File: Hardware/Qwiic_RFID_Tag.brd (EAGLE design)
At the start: 25.4 x 50.8 mm, 49 parts, among them J1 Qwiic, J2 Qwiic, U1 ST25DV64KC

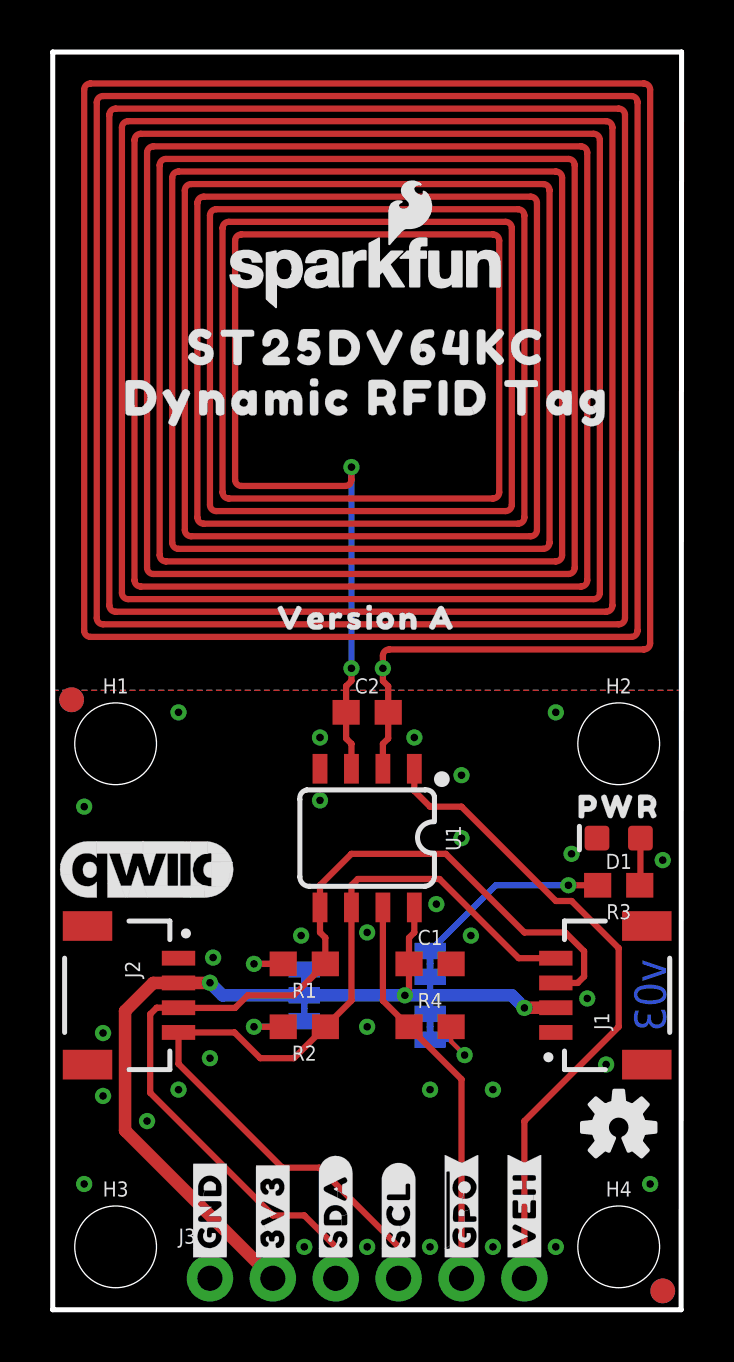
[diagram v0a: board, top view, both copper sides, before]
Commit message: v10 Updates
Remove A and C versions, moving forward with B
Reorganize hardware folder
Rename coil library to match SFE library naming
Bump version number to v10
Smash power symbols to get vector font
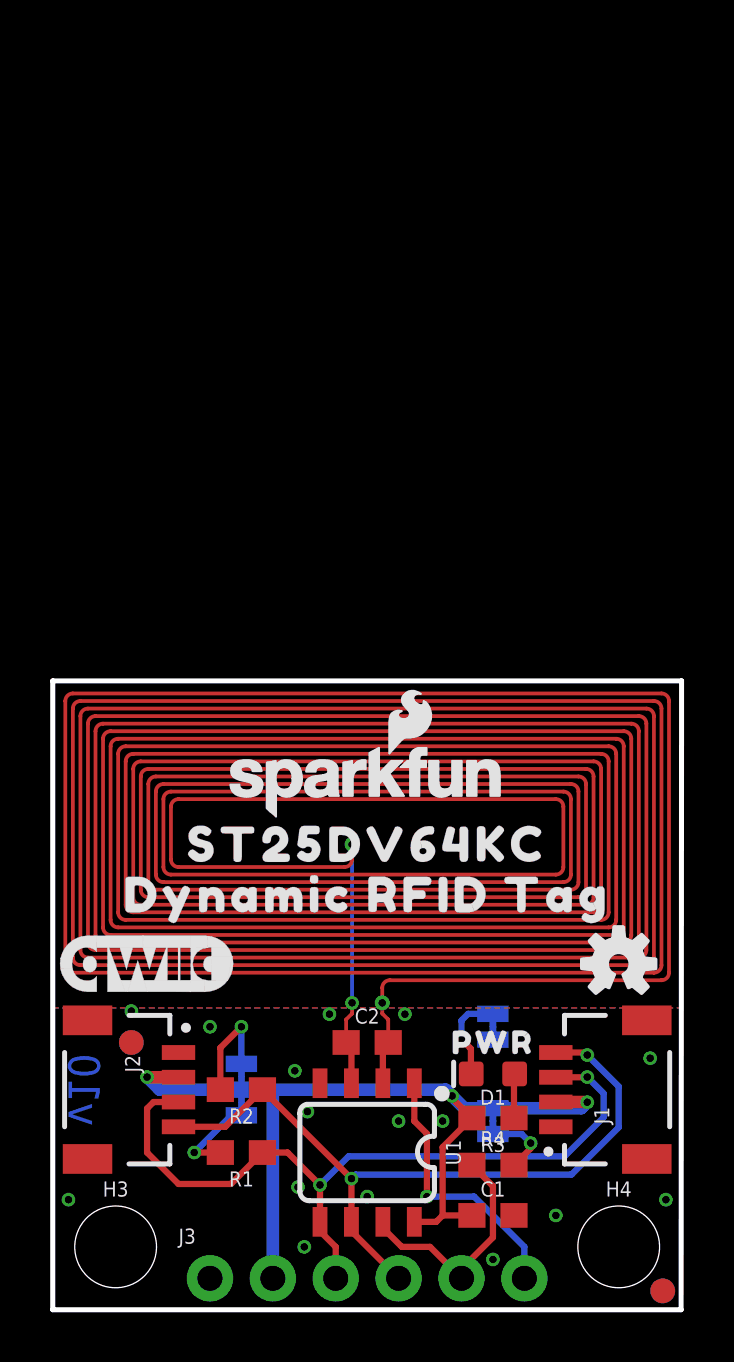
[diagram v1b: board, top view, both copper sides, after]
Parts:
- removed H1, H2: STAND-OFF, SparkFun-Hardware:STAND-OFF
- removed U$12: (no value), output:VERSION_A0
- removed U$2: (no value), output:#3V3#0
- removed U$4: (no value), output:#GND#4
- removed U$5: (no value), output:#SDA#5
- removed U$6: (no value), output:#SCL#6
- removed U$7: (no value), output:##GPO##8
- removed U$8: (no value), output:#VEH#7
- L1: value PCB_COIL_4UH_A -> PCB_COIL_4UH_B; device QWIIC_RFID_TAG_COILS:PCB_COIL_4UH_A -> QWIIC_RFID_TAG_COILS:PCB_COIL_4UH_B
- moved LOGO2 20.6 mm to (12.7, 21.3)
- moved LOGO4 20.6 mm to (12.7, 21.3)
- moved U$13 20.1 mm to (12.7, 18.8)
- moved U$24 20.1 mm to (12.7, 18.8)
- moved U$10 20.1 mm to (12.7, 16.8)
- moved U$11 20.1 mm to (12.7, 16.8)
- moved FD1 14.1 mm to (3.17, 10.8)
- moved FD2 14.1 mm to (3.17, 10.8)
- moved C2 13.3 mm to (12.7, 10.8)
- moved U1 12.7 mm to (12.7, 6.35)
- moved L1 12.7 mm to (12.7, 12.7)
- moved D1 10.8 mm to (17.8, 9.53)
- moved U$9 10.8 mm to (17.8, 10.8)
- moved R3 10.7 mm to (17.8, 7.75)
- moved C1 10.5 mm to (17.8, 3.81)
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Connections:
- net 3.3V: now also R3.2; no longer JP3.2
- net GND: now also JP3.1; no longer D1.C
- net N$1: now also D1.C, JP3.2; no longer JP3.1, R3.2
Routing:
- net VEH: track 26.7 -> 10.8 mm, vias 0 -> 1
- net SDA: track 40.8 -> 31.5 mm, vias 0 -> 2
- net SCL: track 37.2 -> 30.3 mm, vias 0 -> 2
- net !GPO!: track 16.3 -> 9.71 mm
- net N$1: track 7.87 -> 3.70 mm
- net AC1: track 12.4 -> 9.83 mm
- net N$3: track 3.31 -> 4.39 mm
- net AC0: track 4.24 -> 3.43 mm
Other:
- board size 25.4 x 50.8 mm -> 25.4 x 25.4 mm
- board text added: "v10"
- board text removed: "v03"

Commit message: Bump version number to v11 and repanelize
Panelizer didn't work correctly on v10, none of the pads had nets assigned to them, so the GND polygon didn't connect to any GND pads. Repanlizing seems to fix it? Idk, it's whacky.
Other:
- board text added: "v11"
- board text removed: "v10"
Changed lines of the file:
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@@
 <wire x1="25.4" y1="25.4" x2="0" y2="25.4" width="0.2032" layer="20"/>
 <wire x1="0" y1="25.4" x2="0" y2="0" width="0.2032" layer="20"/>
-<text x="1.27" y="8.89" size="1.27" layer="16" font="vector" ratio="15" rot="SMR90" align="center">v10</text>
+<text x="1.27" y="8.89" size="1.27" layer="16" font="vector" ratio="15" rot="SMR90" align="center">v11</text>
 <text x="-8.89" y="-2.54" size="1.524" layer="47" font="vector" align="bottom-center">Units: inches</text>
 <dimension x1="0" y1="0" x2="2.54" y2="0" x3="1.27" y3="-3.81" textsize="1.778" textratio="15" layer="47" unit="inch"/>

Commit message: Remove library file
Part is in SFE Eagle library, update part in design
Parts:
- L1: value PCB_COIL_4UH_B -> PCB_4UH_INDUCTOR-1X0.5; device QWIIC_RFID_TAG_COILS:PCB_COIL_4UH_B -> SparkFun-Coils:PCB_4UH_INDUCTOR_1X0.5
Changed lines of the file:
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@@
 <attribute name="VALUE" x="16.637" y="11.43" size="0.6096" layer="28" font="vector" ratio="20" rot="MR90" align="top-center"/>
 </element>
-<element name="L1" library="QWIIC_RFID_TAG_COILS" package="PCB_COIL_4UH_B" value="PCB_COIL_4UH_B" x="12.7" y="12.7" smashed="yes"/>
+<element name="L1" library="SparkFun-Coils" package="PCB_4UH_INDUCTOR_1X0.5" value="PCB_4UH_INDUCTOR-1X0.5" x="12.7" y="12.7" smashed="yes"/>
 <element name="R1" library="SparkFun-Resistors" package="0603" value="2.2k" x="7.62" y="6.35" smashed="yes" rot="R180">
 <attribute name="NAME" x="7.62" y="5.588" size="0.6096" layer="25" font="vector" ratio="20" rot="R180" align="bottom-center"/>
